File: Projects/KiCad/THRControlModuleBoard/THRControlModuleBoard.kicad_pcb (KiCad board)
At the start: 2 copper layers, 53 parts, among them IC1 LTC1480CN8#PBF, IC2 LTC1480CN8#PBF, J1 Conn_01x02_Socket, J2 Conn_01x02_Socket, J3 Screw_Terminal_01x02, J4 Conn_01x04_Socket, J5 Conn_01x04_Socket, J6 PCC-SMP-K-5, J8 Conn_01x02_Socket, Q1 Q_PMOS_GDS, Q2 Q_PMOS_GDS, Q3 Q_PMOS_GDS, U1 LTC4416EMS#PBF, U2 MAX31856MUD+T

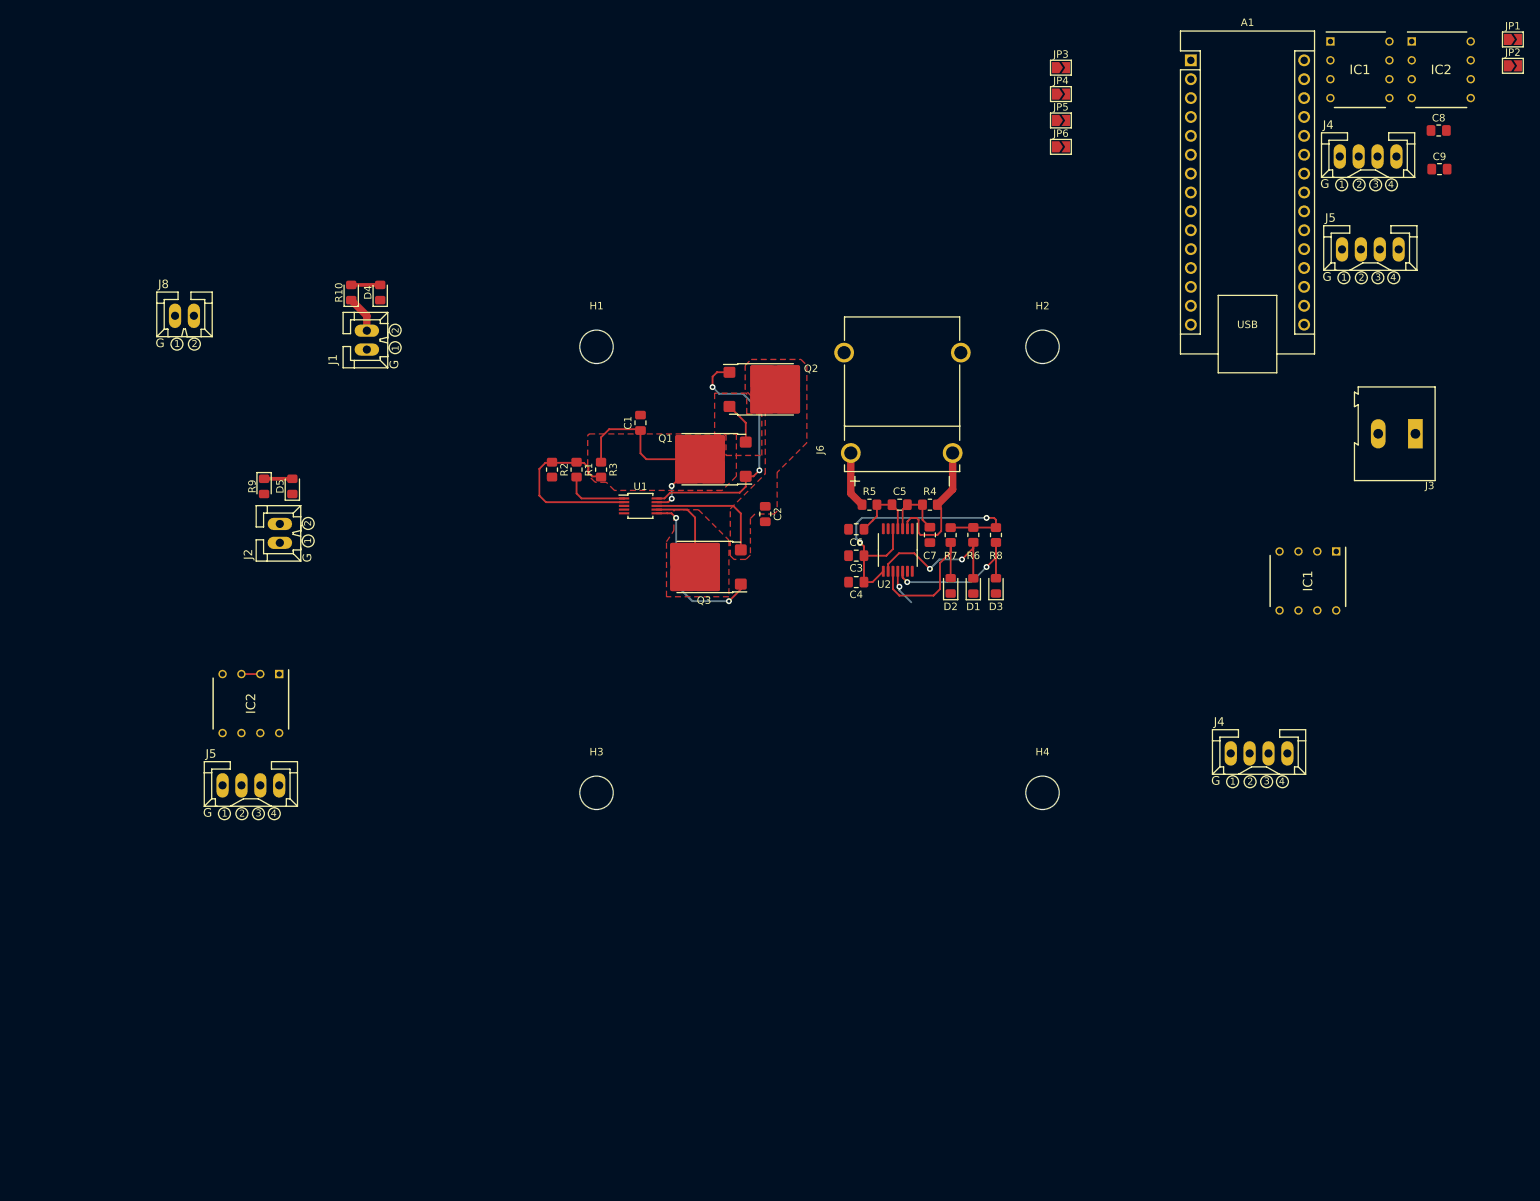
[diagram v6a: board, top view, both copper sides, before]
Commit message: MAX31855、CAN、一部コネクタの追加。 基板形状は供給待ち。
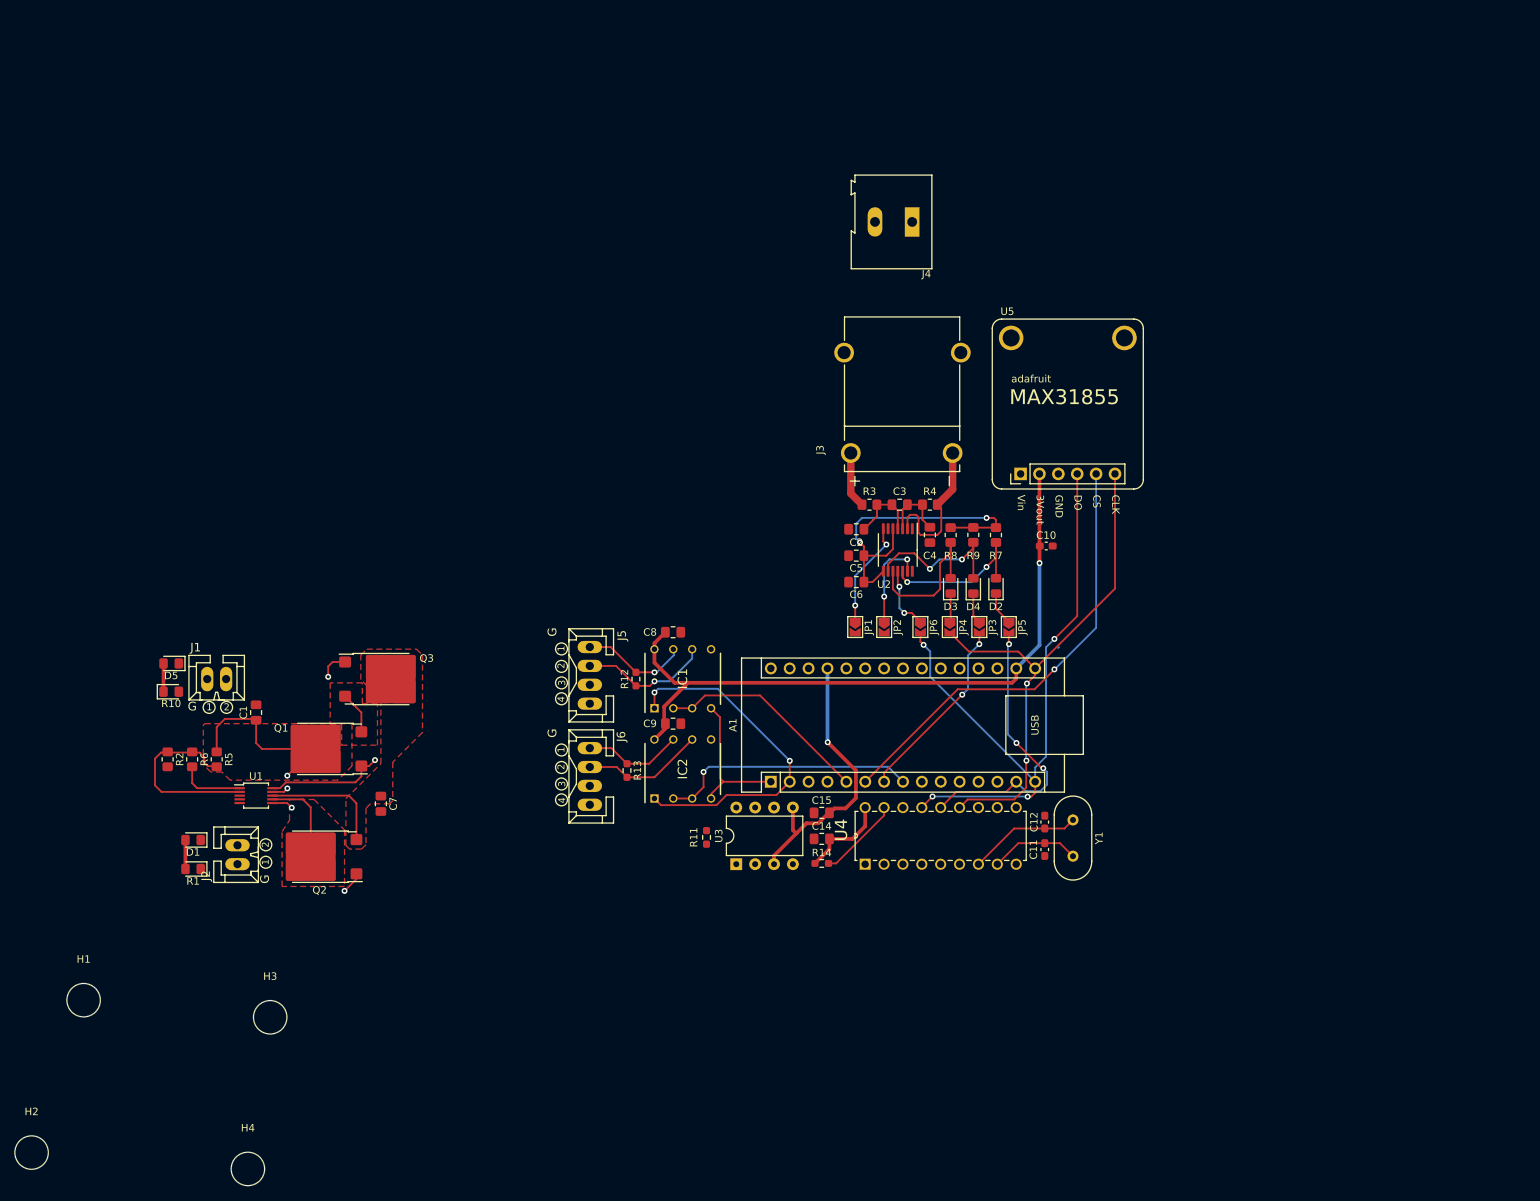
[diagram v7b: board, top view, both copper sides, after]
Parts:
- removed the IC1 at (213.7, 97.6)
- removed the IC2 at (71.5, 114.1)
- removed the J4 at (207.1, 120.8)
- removed the J5 at (71.5, 125.1)
- removed J8: Conn_01x02_Socket, CONNECTOR:CONNECTOR_2-STRAIGHT
- added C10: 0.1μF, Capacitor_SMD:C_0603_1608Metric_Pad1.08x0.95mm_HandSolder, F.Cu at (178.5, 92.9)
- added C11: 15pF, Capacitor_SMD:C_0603_1608Metric_Pad1.08x0.95mm_HandSolder, F.Cu at (178.3, 133.7)
- added C12: 15pF, Capacitor_SMD:C_0603_1608Metric_Pad1.08x0.95mm_HandSolder, F.Cu at (178.3, 130.0)
- added C14: 0.1μF, Capacitor_SMD:C_0805_2012Metric_Pad1.18x1.45mm_HandSolder, F.Cu at (148.3, 132.3)
- added C15: 0.1μF, Capacitor_SMD:C_0805_2012Metric_Pad1.18x1.45mm_HandSolder, F.Cu at (148.3, 128.8)
- added R11: 120Ω, Resistor_SMD:R_0603_1608Metric_Pad0.98x0.95mm_HandSolder, F.Cu at (132.8, 132.1)
- added R12: 120Ω, Resistor_SMD:R_0603_1608Metric_Pad0.98x0.95mm_HandSolder, F.Cu at (123.3, 110.8)
- added R13: 120Ω, Resistor_SMD:R_0603_1608Metric_Pad0.98x0.95mm_HandSolder, F.Cu at (122.1, 123.1)
- added R14: 10kΩ, Resistor_SMD:R_0603_1608Metric_Pad0.98x0.95mm_HandSolder, F.Cu at (148.3, 135.6)
- added U3: Value: MCP2562-E-P, Package_DIP:DIP-8_W7.62mm, F.Cu at (136.8, 135.7)
- added U4: MCP2515-I/P, MCP2515-I_P:DIP254P762X432-18, F.Cu at (174.5, 128.1)
- added U5: MAX31855, MAX31855:MAX31855, F.Cu at (181.4, 62.4)
- added Y1: 8MHz, Crystal:Crystal_HC49-U_Vertical, F.Cu at (182.1, 129.8)
- C8, C9: value 0.1 -> 0.1μF
- moved H2 173.9 mm to (42.0, 174.5)
- moved IC2 138.8 mm to (129.6, 122.9), turned to 90 degrees
- moved C9 127.3 mm to (128.3, 116.8)
- moved J6 126.7 mm to (117.1, 123.9), turned to -90 degrees
- moved J5 125.8 mm to (117.1, 110.3), turned to -90 degrees
- moved C8 123.1 mm to (128.3, 104.5)
- moved IC1 122.5 mm to (129.6, 110.8), turned to 90 degrees
- moved H4 118.3 mm to (71.1, 176.7)
- moved JP1 116.3 mm to (152.8, 103.8), turned to -90 degrees
- moved JP2 115.8 mm to (156.7, 103.8), turned to -90 degrees
- moved A1 112.3 mm to (141.4, 124.6), turned to 90 degrees
- moved H1 111.7 mm to (49.0, 154.0)
- moved R1 80.4 mm to (63.7, 136.3), turned to 180 degrees
- moved D1 77.8 mm to (63.7, 132.4), turned to 180 degrees
- moved JP6 77.6 mm to (161.6, 103.8), turned to -90 degrees
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- renumbered C6 to C2, C5 to C3, C7 to C4, C3 to C5, C4 to C6, C2 to C7, D4 to D1, D3 to D2, D2 to D3, D1 to D4, J6 to J3, J3 to J4, J4 to J5, J5 to J6, JP2 to JP1, JP1 to JP2, JP6 to JP3, JP5 to JP4, JP4 to JP5, JP3 to JP6, Q3 to Q2, Q2 to Q3, R10 to R1, R9 to R10, R5 to R3, R3 to R5, R1 to R6, R8 to R7, R7 to R8, R6 to R9
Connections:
- net /NanoEvery/MAX31856__DRDY-DRDY renamed MAX31856__DRDY-DRDY
- net /NanoEvery/MAX31856__FAULT-FAULT renamed MAX31856__FAULT-FAULT
- net /NanoEvery/SPI__SCK-SCLK renamed SPI__SCLK
- net /NanoEvery/SPI__SDI-MOSI renamed SPI__MOSI
- net /NanoEvery/SPI__SDO-MISO renamed SPI__MISO
- net RS485__A_1 renamed RS485__A1
- net RS485__A_2 renamed RS485__A2
- net RS485__B_1 renamed RS485__B1
- net RS485__B_2 renamed RS485__B2
- A1 pad 17: NanoEvery_3.3V -> +3.3V
- A1 pad 27: unconnected-(A1-+5V-Pad27) -> +5V
- A1 pad 5: RS485__ENABLE -> RS485__ENABLE_B3M
- A1 pad 6: /NanoEvery/MAX31856__~{CS}-~{CS} -> MAX31855__~{CS}-~{CS}
- A1 pad 7: MAX31855__~{CS}-~{CS} -> MAX31856__~{CS}-~{CS}
- A1 pad 8: unconnected-(A1-D5-Pad8) -> RS485__ENABLE_RS405
- A1 pad 9: unconnected-(A1-D6-Pad9) -> MCP2515__~{CS}-~{CS}
- C5 pad 1: NanoEvery_3.3V -> +3.3V
- C6 pad 1: NanoEvery_3.3V -> +3.3V
- C8 pad 1: NanoEvery_3.3V -> +3.3V
- C9 pad 1: NanoEvery_3.3V -> +3.3V
- IC1 pad 2: RS485__ENABLE -> RS485__ENABLE_B3M
- IC1 pad 3: RS485__ENABLE -> RS485__ENABLE_B3M
- IC1 pad 8: NanoEvery_3.3V -> +3.3V
- IC2 pad 2: RS485__ENABLE -> RS485__ENABLE_RS405
- IC2 pad 3: RS485__ENABLE -> RS485__ENABLE_RS405
- IC2 pad 8: NanoEvery_3.3V -> +3.3V
- JP3 pad 2: /NanoEvery/MAX31856__~{CS}-~{CS} -> MAX31856__~{CS}-~{CS}
- R7 pad 1: NanoEvery_3.3V -> +3.3V
- R8 pad 1: NanoEvery_3.3V -> +3.3V
- R9 pad 1: NanoEvery_3.3V -> +3.3V
- U2 pad 5: NanoEvery_3.3V -> +3.3V
- U2 pad 8: NanoEvery_3.3V -> +3.3V
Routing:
- net +3.3V: track 0.00 -> 150.2 mm, vias 0 -> 3
- net SPI__MISO: track 0.00 -> 87.8 mm, vias 0 -> 4
- net SPI__SCLK: track 0.00 -> 70.7 mm, vias 0 -> 2
- net MAX31855__~{CS}-~{CS}: track 0.00 -> 60.5 mm, vias 0 -> 1
- net RS485__RO-RX: track 0.00 -> 47.2 mm, vias 0 -> 2
- net NanoEvery_3.3V: track 44.9 -> 0.00 mm, vias 2 -> 0
- net SPI__MOSI: track 0.00 -> 39.5 mm, vias 0 -> 3
- net +5V: track 0.00 -> 38.1 mm, vias 0 -> 1
- net RS485__ENABLE_RS405: track 0.00 -> 34.7 mm, vias 0 -> 1
- net RS485__ENABLE_B3M: track 0.00 -> 28.8 mm
- net MAX31856__~{CS}-~{CS}: track 0.00 -> 25.4 mm, vias 0 -> 2
- net RS485__DI-TX: track 0.00 -> 19.3 mm
- net RS485__A1: track 0.00 -> 17.6 mm, vias 0 -> 1
- net Net-(Q2-G): track 22.9 -> 5.87 mm
- net RS485__A2: track 0.00 -> 16.4 mm
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
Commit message: PCBにQRコードを追加
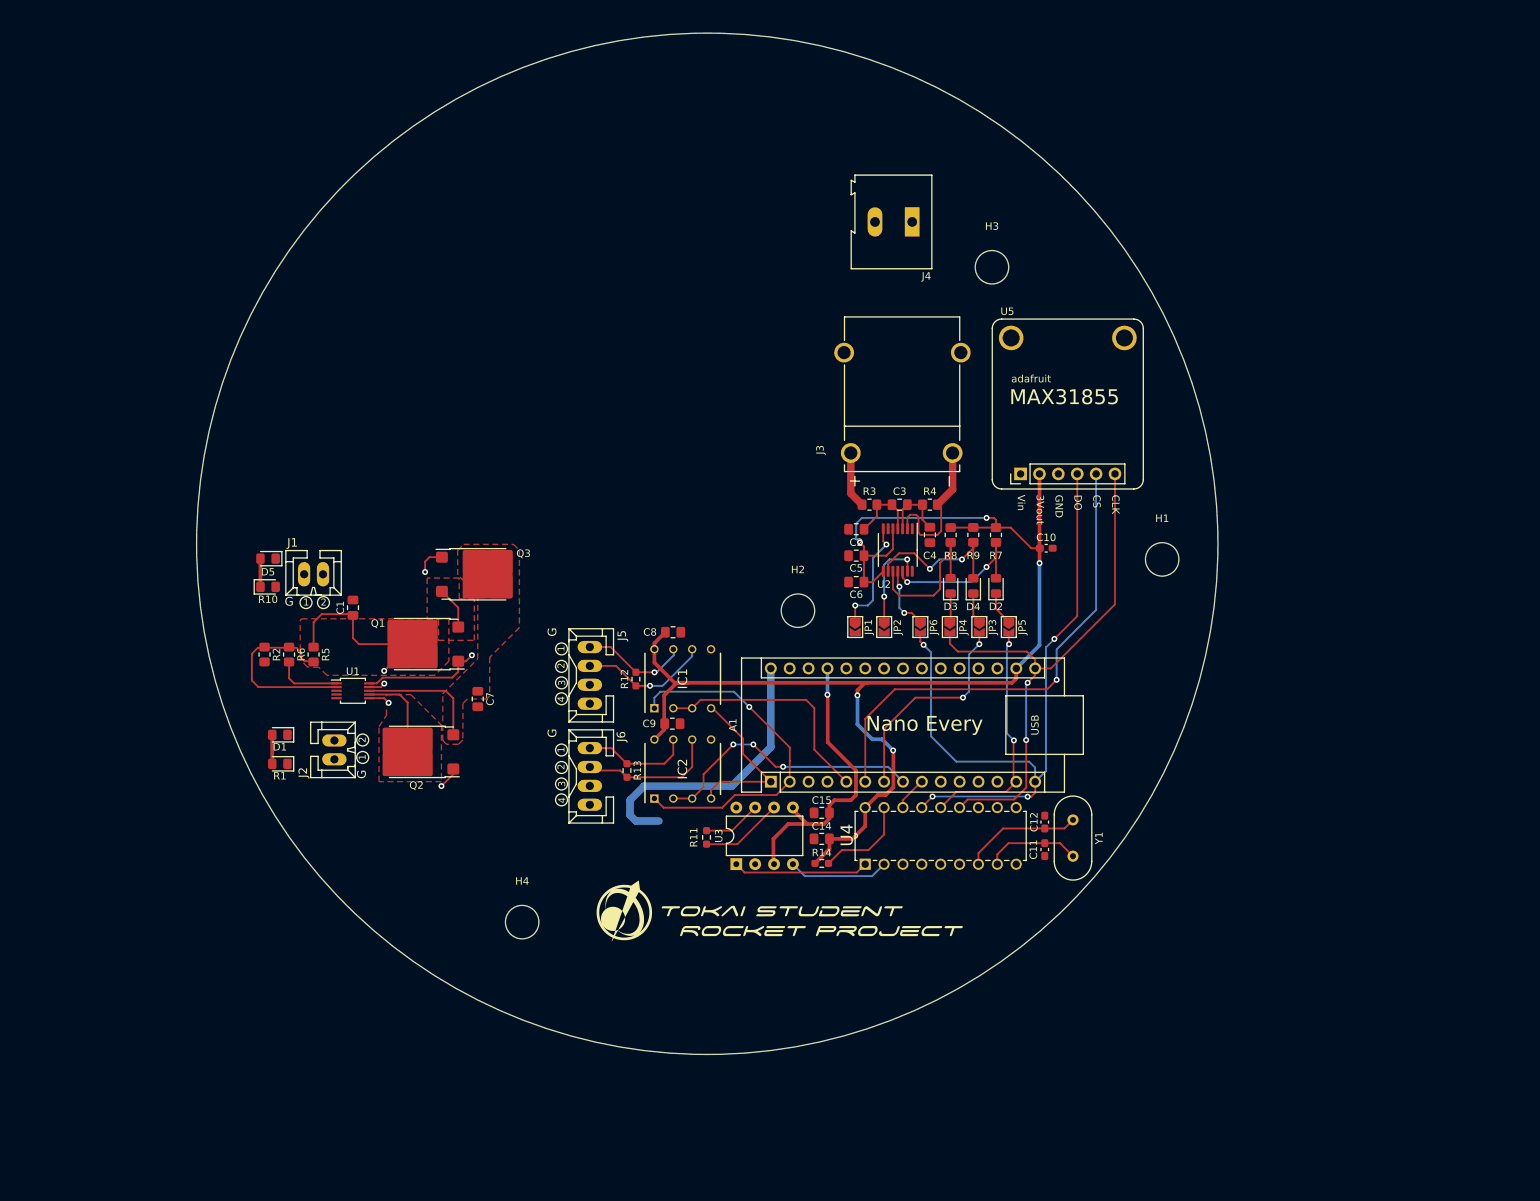
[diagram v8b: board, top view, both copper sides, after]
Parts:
- added G***: LOGO, LOGO, F.Cu at (142.7, 142.1)
- added G***: LOGO, LOGO, B.Cu at (141.1, 132.4)
- moved H1 156.7 mm to (194.1, 94.7)
- moved H3 140.0 mm to (171.2, 55.4)
- moved H2 126.3 mm to (145.1, 101.6)
- moved H4 49.6 mm to (108.0, 143.5)
- moved C1 19.2 mm to (85.2, 101.2)
- moved Q1 19.2 mm to (94.5, 106.1)
- moved Q2 19.2 mm to (93.8, 120.6)
- moved D5 19.2 mm to (73.8, 94.6)
- moved C7 19.2 mm to (102.0, 113.5)
- moved J2 19.2 mm to (82.7, 120.3)
- moved Q3 19.2 mm to (102.2, 96.7)
- moved R5 19.2 mm to (79.9, 107.5)
- moved U1 19.2 mm to (85.2, 112.4)
- moved R10 19.2 mm to (73.8, 98.4)
- moved R2 19.2 mm to (73.3, 107.5)
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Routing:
- net +12V: track 0.00 -> 38.7 mm
- net +3.3V: track 150.2 -> 180.5 mm, vias 3 -> 5
- net CAN__TXD-TXCAN: track 0.00 -> 18.3 mm
- net CAN__RXD-CANRX: track 0.00 -> 13.6 mm
- net CAN_L: track 0.00 -> 11.1 mm
- net CAN_H: track 0.00 -> 7.83 mm
- net SPI__MOSI: track 39.5 -> 32.4 mm, vias 3 -> 2
- net MAX31855__~{CS}-~{CS}: track 60.5 -> 66.3 mm
- net SPI__MISO: track 87.8 -> 93.6 mm
- net MCP2515__~{CS}-~{CS}: track 0.00 -> 4.60 mm
- net MAX31856__~{CS}-~{CS}: track 25.4 -> 29.1 mm
- net RS485__DI-TX: track 19.3 -> 22.9 mm
- net RS485__ENABLE_B3M: track 28.8 -> 31.6 mm
- net SPI__SCLK: track 70.7 -> 73.5 mm
- net RS485__ENABLE_RS405: track 34.7 -> 37.0 mm, vias 1 -> 3
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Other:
- board outline added: 137.4 x 137.4 mm
- board text added: "Nano Every"
